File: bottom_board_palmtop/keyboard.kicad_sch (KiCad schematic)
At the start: 36 parts, among them Q1 2N7002DW-7-F, SW1 KeebDeck_individual_keys, U10 TPAZ1043-04F, U11 TPAZ1043-04F, U12 TPAZ1043-04F, U13 TPAZ1043-04F, U14 TPAZ1043-04F, U15 TPAZ1043-04F, U16 TPAZ1043-04F, U17 TPAZ1043-04F, U18 TPAZ1043-04F, U19 TPAZ1043-04F, U2 TPAZ1043-04F, U20 TPAZ1043-04F, U4 TPAZ1043-04F, U7 TPAZ1043-04F, U8 TPAZ1043-04F, U9 TPAZ1043-04F

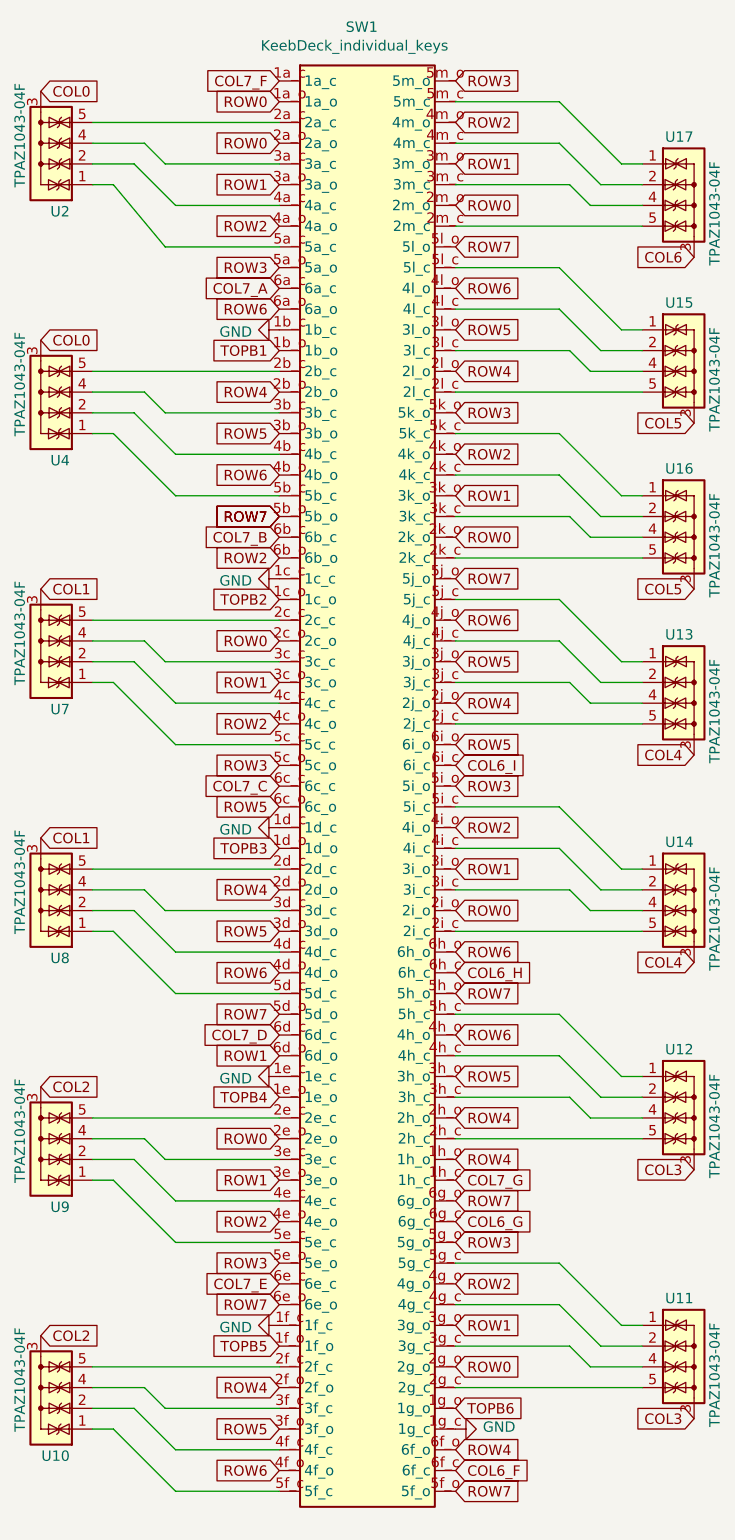
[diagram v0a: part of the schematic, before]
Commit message: bottom_board_palmtop: JLC PCBA preparation; clarifying I2C addresses in use
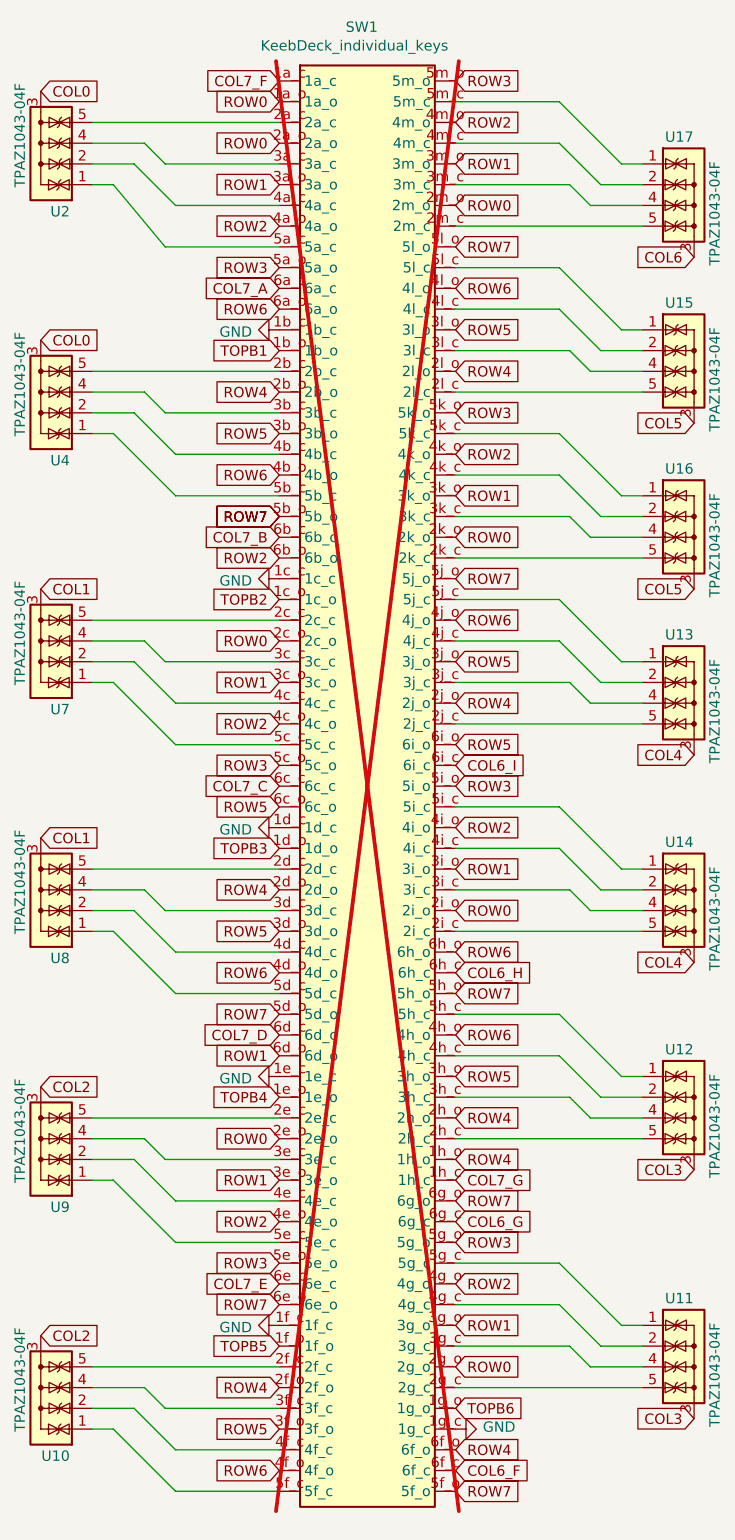
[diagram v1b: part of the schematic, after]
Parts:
- SW1: now not fitted; now left out of the parts list
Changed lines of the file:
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@@
 		(unit 1)
 		(exclude_from_sim no)
-		(in_bom yes)
+		(in_bom no)
 		(on_board yes)
-		(dnp no)
+		(dnp yes)
 		(property "Reference" "SW1"
 			(at 114.808 12.446 0)
